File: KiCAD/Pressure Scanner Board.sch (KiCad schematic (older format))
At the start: 17 parts, among them J1 Cortex_Debug, SW1 FSMCTTR, U1 SAMD21G18A-AU, Y1 32.768kHz

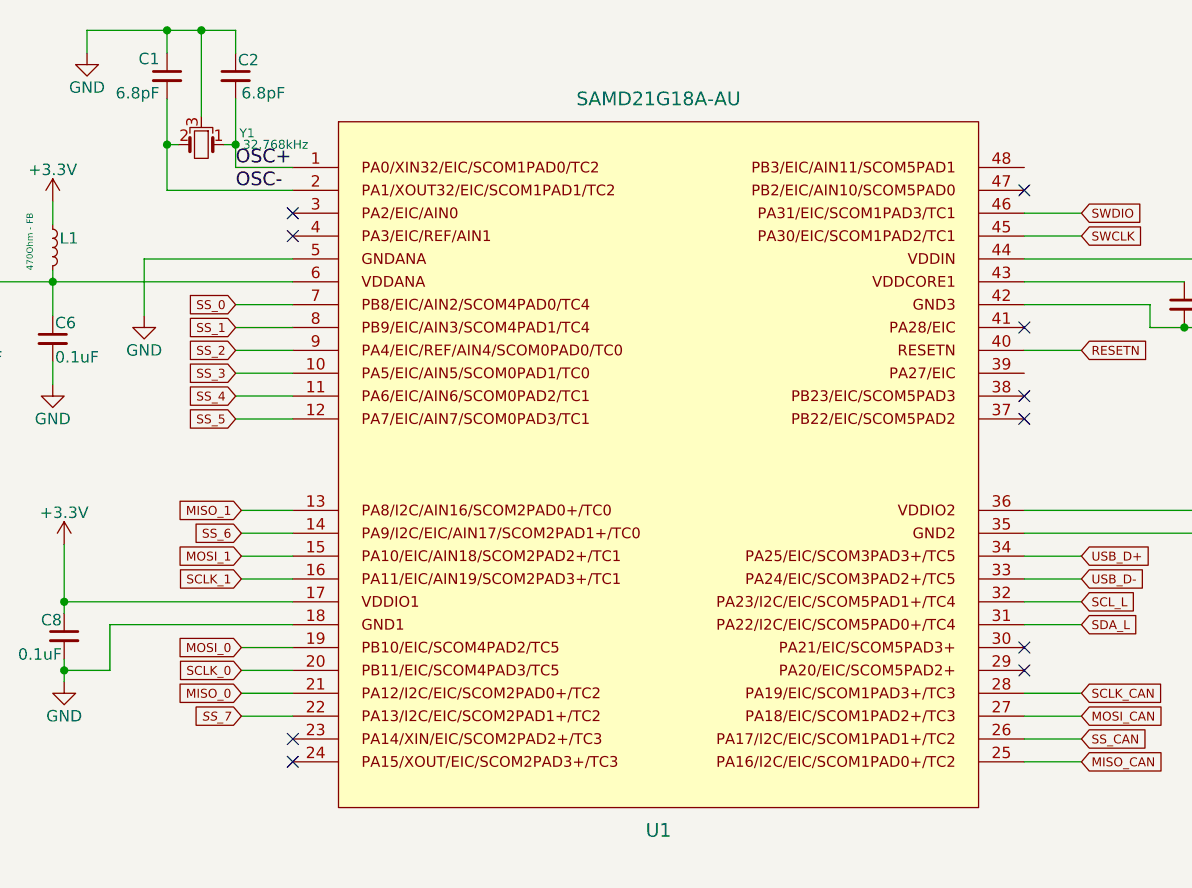
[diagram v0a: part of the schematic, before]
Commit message: Dropped 4 spare sensors, revising layout.
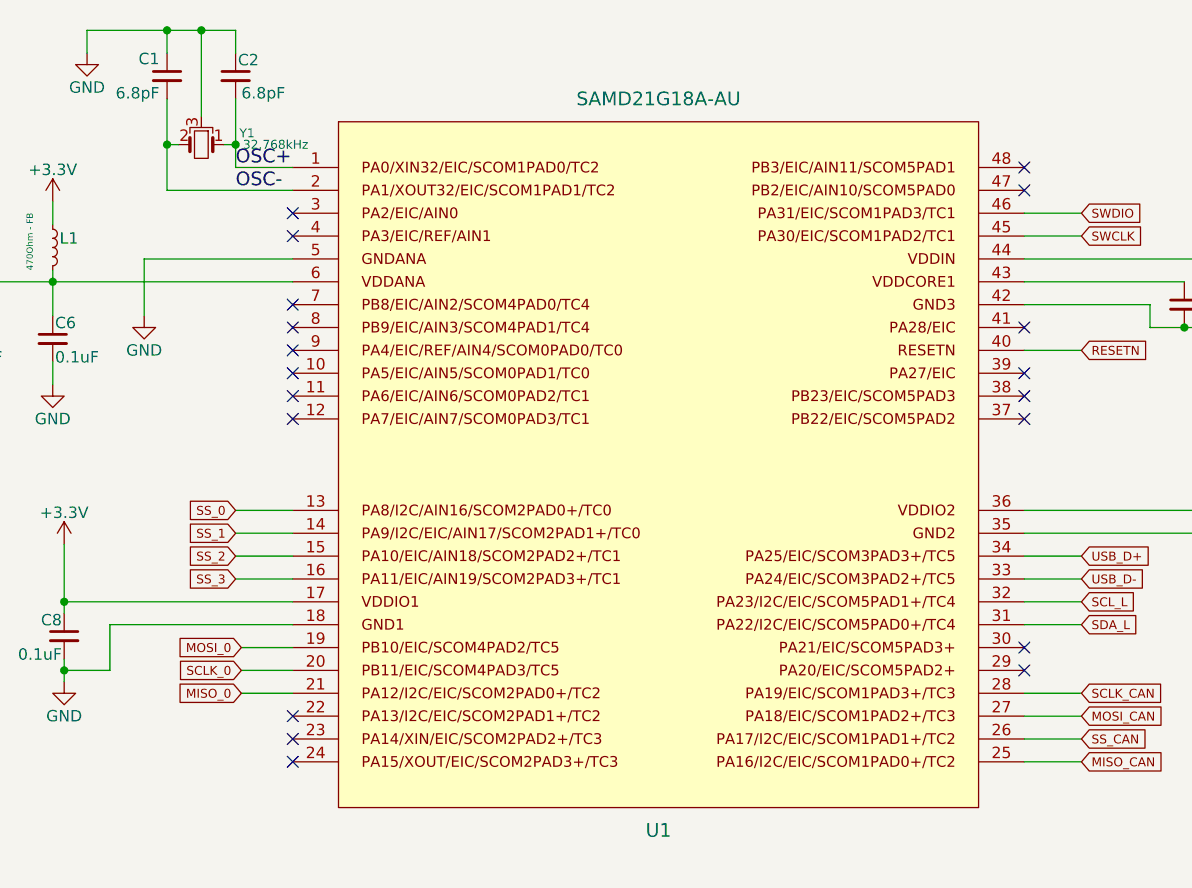
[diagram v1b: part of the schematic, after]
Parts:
- C1, C2: footprint Capacitors_SMD:C_0805 -> Capacitors_SMD:C_0603
- C3, C4, C6, C7, C8: footprint Capacitors_SMD:C_1206 -> Capacitors_SMD:C_0603
- L1: footprint Inductors_SMD:L_1806 -> Inductors_SMD:L_0603
- R1, R2: footprint Resistors_SMD:R_1210 -> Resistors_SMD:R_0603
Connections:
- net MISO_1 is gone; now on net SS_0: U1.13
- net MOSI_1 is gone; now on net SS_2: U1.15
- net SCLK_1 is gone; now on net SS_3: U1.16
- net SS_6 is gone; now on net SS_1: U1.14
- net SS_0: no longer U1.7
- net SS_1: no longer U1.8
- net SS_2: no longer U1.9
- net SS_3: no longer U1.10
- net SS_4: no longer names the net of U1.11
- net SS_5: no longer names the net of U1.12
- net SS_7: no longer names the net of U1.22
- no-connect marks 14 -> 23
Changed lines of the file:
@@
 F 0 "C1" H 2225 1475 50  0000 L CNN
 F 1 "6.8pF" H 2125 1325 50  0000 L CNN
-F 2 "Capacitors_SMD:C_0805" H 2350 1400 50  0001 C CNN
+F 2 "Capacitors_SMD:C_0603" H 2350 1400 50  0001 C CNN
 F 3 "" H 2350 1400 50  0001 C CNN
 	1    2350 1400
@@
 F 0 "C2" H 2660 1470 50  0000 L CNN
 F 1 "6.8pF" H 2675 1325 50  0000 L CNN
-F 2 "Capacitors_SMD:C_0805" H 2650 1400 50  0001 C CNN
+F 2 "Capacitors_SMD:C_0603" H 2650 1400 50  0001 C CNN
 F 3 "" H 2650 1400 50  0001 C CNN
 	1    2650 1400
@@
 F 0 "C3" H 6900 2475 50  0000 L CNN
 F 1 "0.1uF" H 6900 2400 50  0000 L CNN
-F 2 "Capacitors_SMD:C_1206" H 6800 2400 50  0001 C CNN
+F 2 "Capacitors_SMD:C_0603" H 6800 2400 50  0001 C CNN
 F 3 "" H 6800 2400 50  0001 C CNN
 	1    6800 2400
@@
 F 0 "C8" H 1910 3920 50  0000 L CNN
 F 1 "0.1uF" H 1910 3770 50  0000 L CNN
-F 2 "Capacitors_SMD:C_1206" H 1900 3850 50  0001 C CNN
+F 2 "Capacitors_SMD:C_0603" H 1900 3850 50  0001 C CNN
 F 3 "" H 1900 3850 50  0001 C CNN
 	1    1900 3850
@@
 F 0 "C4" H 7260 2470 50  0000 L CNN
 F 1 "0.1uF" H 7260 2320 50  0000 L CNN
-F 2 "Capacitors_SMD:C_1206" H 7250 2400 50  0001 C CNN
+F 2 "Capacitors_SMD:C_0603" H 7250 2400 50  0001 C CNN
 F 3 "" H 7250 2400 50  0001 C CNN
 	1    7250 2400
@@
 F 0 "L1" H 1880 2190 50  0000 L CNN
 F 1 "470Ohm - FB" V 1750 2050 28  0000 L CNN
-F 2 "Inductors_SMD:L_1806" H 1850 2150 50  0001 C CNN
+F 2 "Inductors_SMD:L_0603" H 1850 2150 50  0001 C CNN
 F 3 "" H 1850 2150 50  0001 C CNN
 	1    1850 2150
@@
 F 0 "C6" H 1860 2620 50  0000 L CNN
 F 1 "0.1uF" H 1860 2470 50  0000 L CNN
-F 2 "Capacitors_SMD:C_1206" H 1850 2550 50  0001 C CNN
+F 2 "Capacitors_SMD:C_0603" H 1850 2550 50  0001 C CNN
 F 3 "" H 1850 2550 50  0001 C CNN
 	1    1850 2550
@@
 F 0 "R1" V 8630 1650 50  0000 C CNN
 F 1 "10k" V 8550 1650 50  0000 C CNN
-F 2 "Resistors_SMD:R_1210" V 8480 1650 50  0001 C CNN
+F 2 "Resistors_SMD:R_0603" V 8480 1650 50  0001 C CNN
 F 3 "" H 8550 1650 50  0001 C CNN
 	1    8550 1650
@@
 F 0 "R2" V 8280 5150 50  0000 C CNN
 F 1 "330" V 8200 5150 50  0000 C CNN
-F 2 "Resistors_SMD:R_1210" V 8130 5150 50  0001 C CNN
+F 2 "Resistors_SMD:R_0603" V 8130 5150 50  0001 C CNN
 F 3 "" H 8200 5150 50  0001 C CNN
 	1    8200 5150
@@
 F 0 "C7" H 7260 3520 50  0000 L CNN
 F 1 "0.1uF" H 7260 3370 50  0000 L CNN
-F 2 "Capacitors_SMD:C_1206" H 7250 3450 50  0001 C CNN
+F 2 "Capacitors_SMD:C_0603" H 7250 3450 50  0001 C CNN
 F 3 "" H 7250 3450 50  0001 C CNN
 	1    7250 3450
@@
 Text GLabel 6350 4100 2    39   Input ~ 0
 SCLK_CAN
-Text GLabel 2675 3300 0    39   Input ~ 0
-MISO_1
-Text GLabel 2675 3500 0    39   Input ~ 0
-MOSI_1
-Text GLabel 2675 3600 0    39   Input ~ 0
-SCLK_1
 Text GLabel 2675 3900 0    39   Input ~ 0
 MOSI_0
@@
 Text GLabel 6350 3700 2    39   Input ~ 0
 SCL_L
-Text GLabel 2650 2400 0    39   Input ~ 0
+Text GLabel 2650 3300 0    39   Input ~ 0
 SS_0
-Text GLabel 2650 2500 0    39   Input ~ 0
+Text GLabel 2650 3400 0    39   Input ~ 0
 SS_1
-Text GLabel 2650 2600 0    39   Input ~ 0
+Text GLabel 2650 3500 0    39   Input ~ 0
 SS_2
-Text GLabel 2650 2700 0    39   Input ~ 0
+Text GLabel 2650 3600 0    39   Input ~ 0
 SS_3
-Text GLabel 2650 2800 0    39   Input ~ 0
-SS_4
-Text GLabel 2650 2900 0    39   Input ~ 0
-SS_5
-Text GLabel 2675 3400 0    39   Input ~ 0
-SS_6
-Text GLabel 2675 4200 0    39   Input Italic 0
-SS_7
 Wire Wire Line
 	8650 4050 8650 3900
@@
 	6100 4200 6350 4200
 Wire Wire Line
-	2675 3300 2900 3300
-Wire Wire Line
-	2675 3500 2900 3500
-Wire Wire Line
-	2675 3600 2900 3600
-Wire Wire Line
 	2675 3900 2900 3900
 Wire Wire Line
@@
 	6100 3800 6350 3800
 Wire Wire Line
-	2675 4200 2900 4200
-Wire Wire Line
-	2675 3400 2900 3400
-Wire Wire Line
-	2650 2900 2900 2900
-Wire Wire Line
-	2650 2800 2900 2800
-Wire Wire Line
-	2650 2700 2900 2700
-Wire Wire Line
-	2650 2600 2900 2600
-Wire Wire Line
-	2650 2500 2900 2500
-Wire Wire Line
-	2650 2400 2900 2400
+	2650 3600 2900 3600
+Wire Wire Line
+	2650 3500 2900 3500
+Wire Wire Line
+	2650 3400 2900 3400
+Wire Wire Line
+	2650 3300 2900 3300
 NoConn ~ 2900 2000
 NoConn ~ 2900 2100
@@
 Text Label 2650 1900 0    60   ~ 0
 OSC-
+NoConn ~ 2900 4200
+NoConn ~ 2900 2900
+NoConn ~ 2900 2400
+NoConn ~ 2900 2500
+NoConn ~ 2900 2600
+NoConn ~ 2900 2700
+NoConn ~ 2900 2800
+NoConn ~ 6100 2700
+NoConn ~ 6100 1800
 $EndSCHEMATC
